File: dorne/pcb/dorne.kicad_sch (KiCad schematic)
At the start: 96 parts, among them J1 MJ-4PP-9, J2 MJ-4PP-9, SW1 SW_PUSH, SW10 SW_PUSH, SW11 SW_PUSH, SW12 SW_PUSH, SW13 SW_PUSH, SW14 SW_PUSH, SW15 SW_PUSH, SW16 SW_PUSH, SW17 SW_PUSH, SW18 SW_PUSH, SW19 SW_PUSH, SW2 SW_PUSH, SW20 SW_PUSH, SW21 SW_PUSH, SW22 SW_PUSH, SW23 SW_PUSH, SW24 SW_PUSH, SW25 SW_PUSH, SW26 SW_PUSH, SW27 SW_PUSH, SW28 SW_PUSH, SW29 SW_PUSH, SW3 SW_PUSH, SW30 SW_PUSH, SW31 SW_PUSH, SW32 SW_PUSH, SW33 SW_PUSH, SW34 SW_PUSH, SW35 SW_PUSH, SW36 SW_PUSH, SW37 SW_PUSH, SW38 SW_PUSH, SW39 SW_PUSH, SW4 SW_PUSH, SW40 SW_PUSH, SW41 SW_PUSH, SW42 SW_PUSH, SW5 SW_PUSH, SW6 SW_PUSH, SW7 SW_PUSH, SW8 SW_PUSH, SW9 SW_PUSH, U3 nice_nano, U4 nice_nano

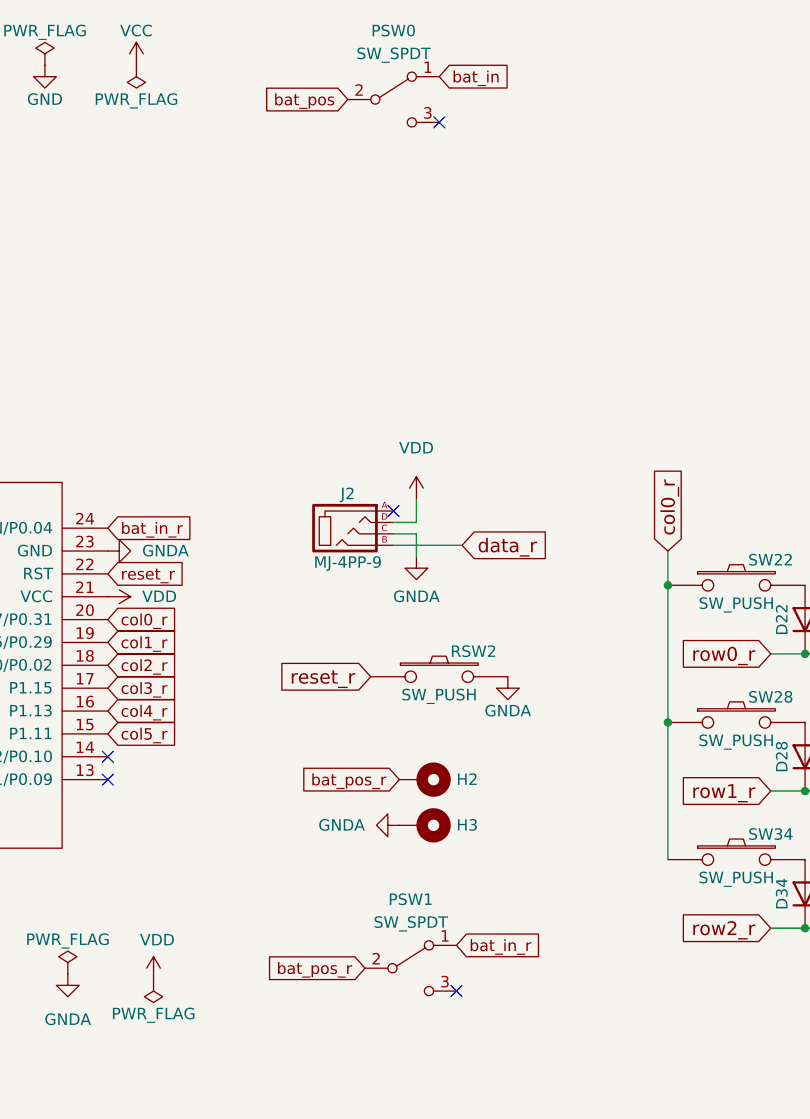
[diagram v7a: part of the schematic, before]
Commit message: Trying to fix the edge cuts and add back in the M2 holes
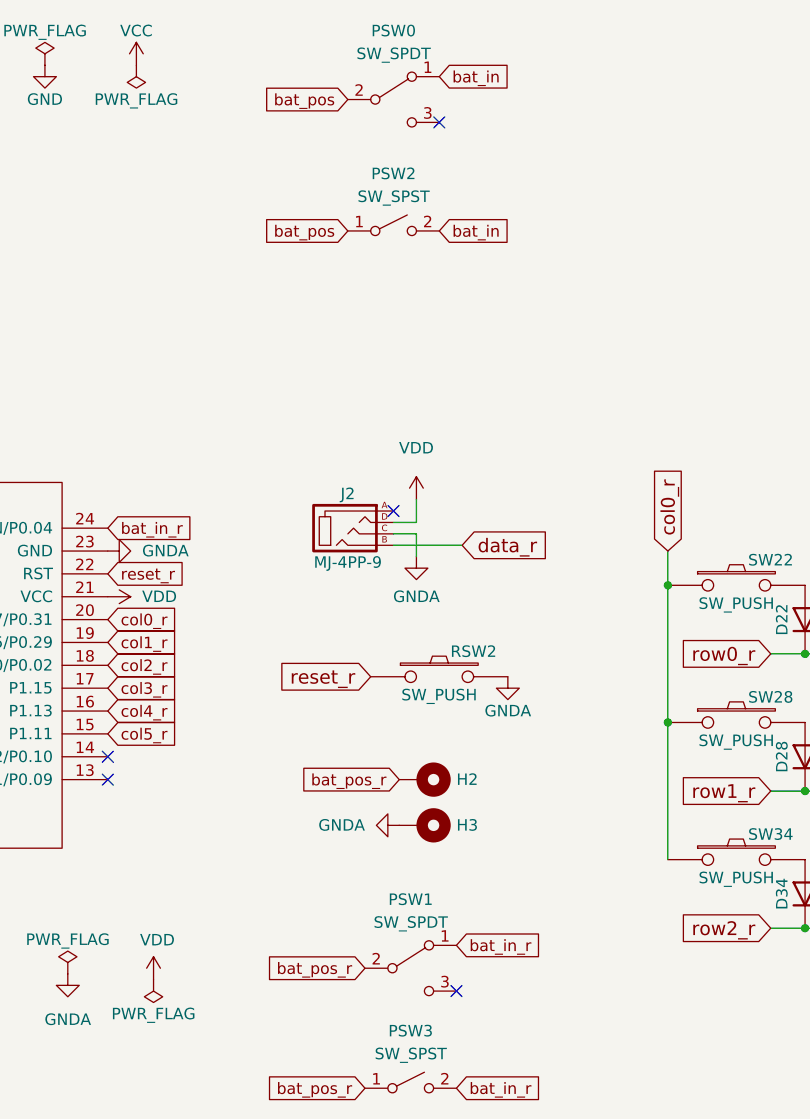
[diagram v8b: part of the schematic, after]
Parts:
- added PSW2, PSW3: SW_SPST, buttons:SW_L068-A, symbol Switch:SW_SPST
- RSW1, RSW2: footprint Button_Switch_SMD:SW_Push_SPST_NO_Alps_SKRK -> lib:CK_Components-KSR223GNCLFG-0
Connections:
- net bat_in: now also PSW2.2 (B)
- net bat_in_r: now also PSW3.2 (B)
- net bat_pos: now also PSW2.1 (A)
- net bat_pos_r: now also PSW3.1 (A)
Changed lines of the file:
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@@
+    )
+  )
+  (global_label "bat_pos_r" (shape input) (at 99.695 193.675 180) (fields_autoplaced)
+    (effects (font (size 1.27 1.27)) (justify right))
+    (property "Intersheet References" "${INTERSHEET_REFS}" (id 0) (at 88.2994 193.5956 0)
+      (effects (font (size 1.27 1.27)) (justify right) hide)
     )
   )
@@
     )
   )
+  (global_label "bat_pos" (shape input) (at 97.79 98.425 180) (fields_autoplaced)
+    (effects (font (size 1.27 1.27)) (justify right))
+    (property "Intersheet References" "${INTERSHEET_REFS}" (id 0) (at 88.1482 98.3456 0)
+      (effects (font (size 1.27 1.27)) (justify right) hide)
+    )
+  )
   (global_label "col2" (shape input) (at 71.12 48.26 0) (fields_autoplaced)
     (effects (font (size 1.27 1.27)) (justify left))
@@
     )
   )
+  (global_label "bat_in" (shape input) (at 107.95 98.425 0) (fields_autoplaced)
+    (effects (font (size 1.27 1.27)) (justify left))
+    (property "Intersheet References" "${INTERSHEET_REFS}" (id 0) (at 116.0194 98.3456 0)
+      (effects (font (size 1.27 1.27)) (justify left) hide)
+    )
+  )
   (global_label "col2_r" (shape input) (at 168.91 133.985 90) (fields_autoplaced)
     (effects (font (size 1.524 1.524)) (justify left))
@@
     )
   )
+  (global_label "bat_in_r" (shape input) (at 109.855 193.675 0) (fields_autoplaced)
+    (effects (font (size 1.27 1.27)) (justify left))
+    (property "Intersheet References" "${INTERSHEET_REFS}" (id 0) (at 119.6782 193.5956 0)
+      (effects (font (size 1.27 1.27)) (justify left) hide)
+    )
+  )
   (global_label "data" (shape input) (at 107.315 33.02 0) (fields_autoplaced)
     (effects (font (size 1.524 1.524)) (justify left))
@@
     (property "Reference" "RSW1" (id 0) (at 108.585 46.101 0))
     (property "Value" "SW_PUSH" (id 1) (at 104.775 50.927 0))
-    (property "Footprint" "Button_Switch_SMD:SW_Push_SPST_NO_Alps_SKRK" (id 2) (at 104.775 48.895 0)
+    (property "Footprint" "lib:CK_Components-KSR223GNCLFG-0" (id 2) (at 104.775 48.895 0)
       (effects (font (size 1.27 1.27)) hide)
     )
@@
     (property "Reference" "RSW2" (id 0) (at 111.76 145.161 0))
     (property "Value" "SW_PUSH" (id 1) (at 107.95 149.987 0))
-    (property "Footprint" "Button_Switch_SMD:SW_Push_SPST_NO_Alps_SKRK" (id 2) (at 107.95 147.955 0)
+    (property "Footprint" "lib:CK_Components-KSR223GNCLFG-0" (id 2) (at 107.95 147.955 0)
       (effects (font (size 1.27 1.27)) hide)
     )
@@
     (pin "1")
   )
+  (symbol (lib_id "Switch:SW_SPST") (at 102.87 98.425 0) (unit 1)
+    (in_bom yes) (on_board yes) (fields_autoplaced)
+    (property "Reference" "PSW2" (id 0) (at 102.87 92.075 0))
+    (property "Value" "SW_SPST" (id 1) (at 102.87 94.615 0))
+    (property "Footprint" "buttons:SW_L068-A" (id 2) (at 102.87 98.425 0)
+      (effects (font (size 1.27 1.27)) hide)
+    )
+    (property "Datasheet" "~" (id 3) (at 102.87 98.425 0)
+      (effects (font (size 1.27 1.27)) hide)
+    )
+    (pin "1")
+    (pin "2")
+  )
   (symbol (lib_name "VDD_1") (lib_id "power:VDD") (at 71.12 139.065 270) (unit 1)
     (in_bom yes) (on_board yes) (fields_autoplaced)
@@
     (pin "1")
   )
+  (symbol (lib_id "Switch:SW_SPST") (at 104.775 193.675 0) (unit 1)
+    (in_bom yes) (on_board yes) (fields_autoplaced)
+    (property "Reference" "PSW3" (id 0) (at 104.775 187.325 0))
+    (property "Value" "SW_SPST" (id 1) (at 104.775 189.865 0))
+    (property "Footprint" "buttons:SW_L068-A" (id 2) (at 104.775 193.675 0)
+      (effects (font (size 1.27 1.27)) hide)
+    )
+    (property "Datasheet" "~" (id 3) (at 104.775 193.675 0)
+      (effects (font (size 1.27 1.27)) hide)
+    )
+    (pin "1")
+    (pin "2")
+  )
   (symbol (lib_id "power:PWR_FLAG") (at 66.675 180.975 0) (unit 1)
     (in_bom yes) (on_board yes)
@@
       (reference "PSW1") (unit 1) (value "SW_SPDT") (footprint "lib:ALPS-SSSS811101-0")
     )
+    (path "/645feb5b-b062-4aac-b332-0cae328d9cdb"
+      (reference "PSW2") (unit 1) (value "SW_SPST") (footprint "buttons:SW_L068-A")
+    )
+    (path "/af8ab7f2-d879-463f-abae-8b515b22ec62"
+      (reference "PSW3") (unit 1) (value "SW_SPST") (footprint "buttons:SW_L068-A")
+    )
     (path "/00000000-0000-0000-0000-00005a5eb9e2"
-      (reference "RSW1") (unit 1) (value "SW_PUSH") (footprint "Button_Switch_SMD:SW_Push_SPST_NO_Alps_SKRK")
+      (reference "RSW1") (unit 1) (value "SW_PUSH") (footprint "lib:CK_Components-KSR223GNCLFG-0")
     )
     (path "/00000000-0000-0000-0000-00005c25f978"
-      (reference "RSW2") (unit 1) (value "SW_PUSH") (footprint "Button_Switch_SMD:SW_Push_SPST_NO_Alps_SKRK")
+      (reference "RSW2") (unit 1) (value "SW_PUSH") (footprint "lib:CK_Components-KSR223GNCLFG-0")
     )
     (path "/00000000-0000-0000-0000-00005a5e2b19"
